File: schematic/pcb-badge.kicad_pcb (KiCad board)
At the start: 2 copper layers, 71.8 x 81.3 mm, 7 parts, among them SW1 SW_Push

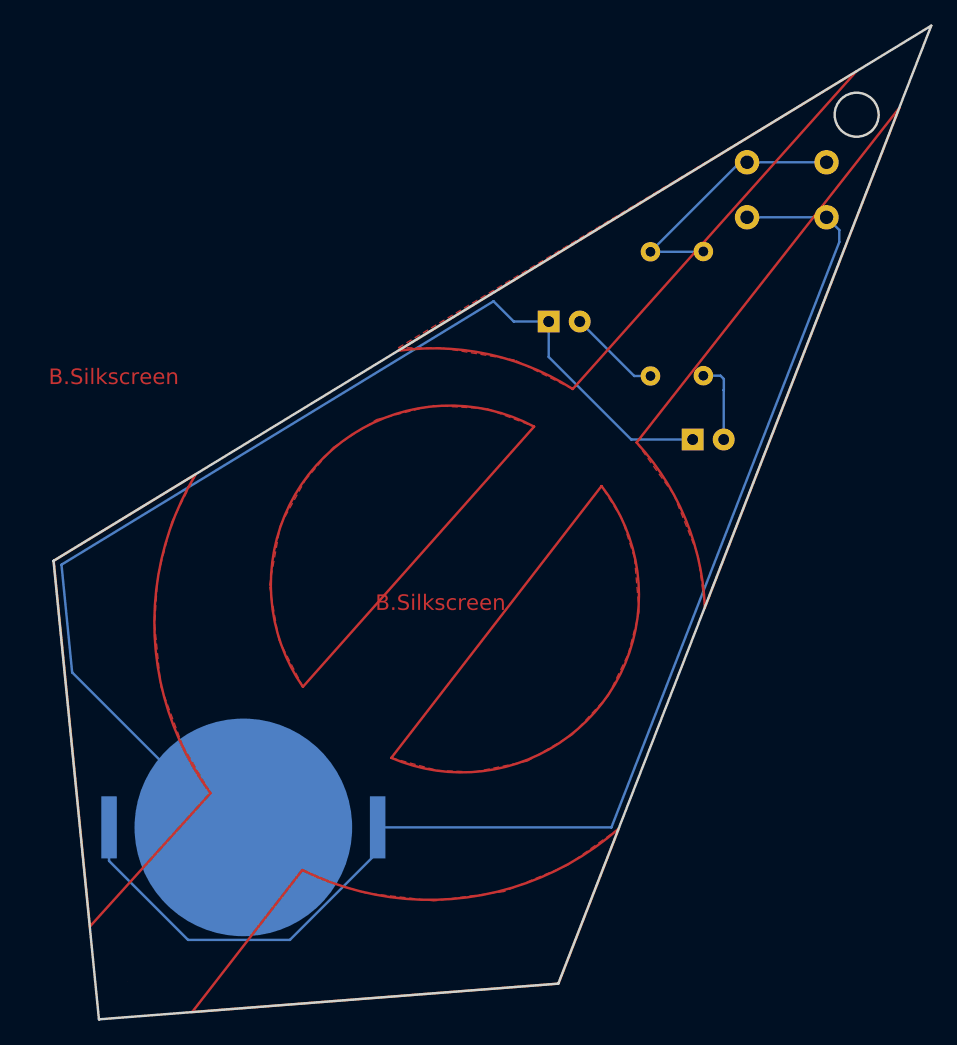
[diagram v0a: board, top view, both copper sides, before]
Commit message: fixed traces
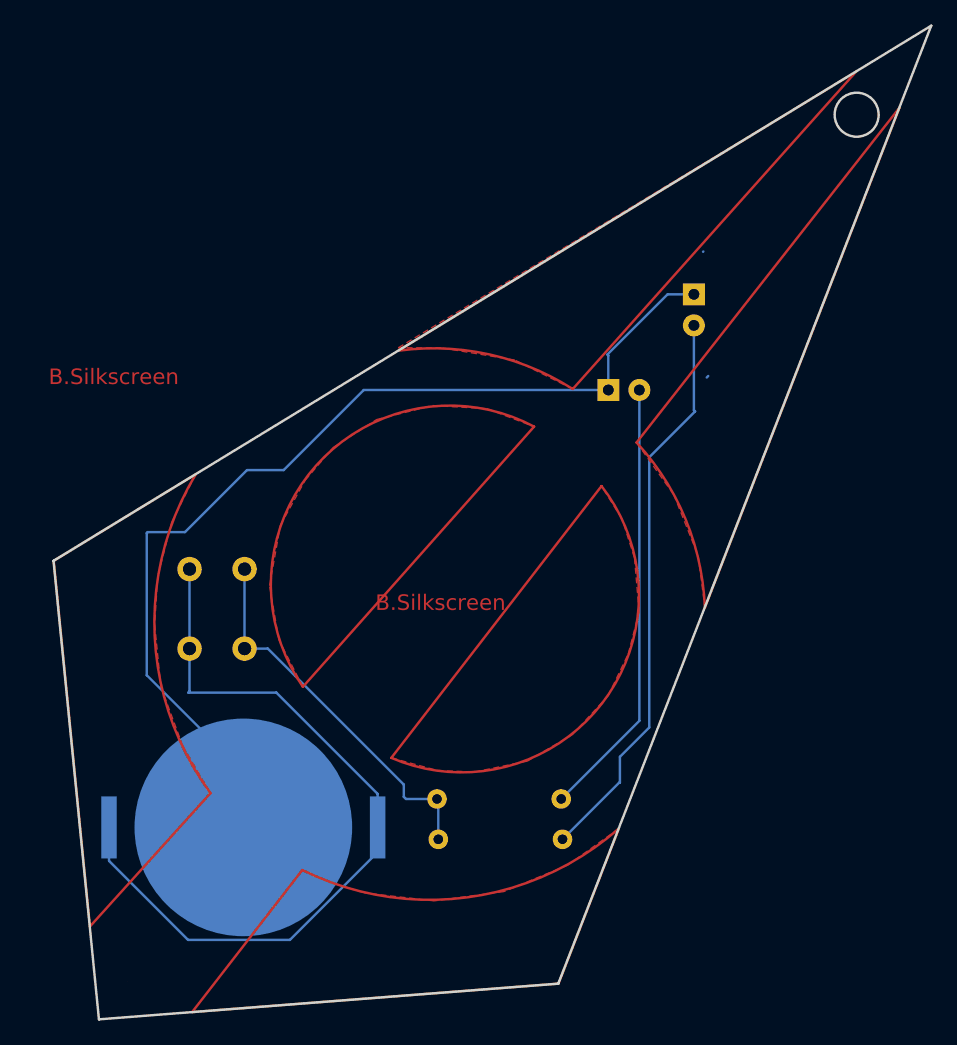
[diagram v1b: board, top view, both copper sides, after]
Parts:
- moved SW1 62.0 mm to (184.9, 81.6), turned to 90 degrees
- moved R2 52.7 mm to (200.7, 97.2), turned to 0 degrees
- moved R1 48.0 mm to (200.6, 93.9), turned to 0 degrees
- moved D2 11.9 mm to (221.7, 52.6), turned to -90 degrees
- moved D1 7.42 mm to (214.7, 60.5)
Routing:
- net VCC: track 111.8 -> 64.4 mm
- net Net-(D2-A): track 6.92 -> 46.6 mm
- net Net-(D1-A): track 7.63 -> 36.1 mm
- net Net-(R1-Pad1): track 21.8 -> 31.3 mm
- net GND: track 92.2 -> 83.3 mm
